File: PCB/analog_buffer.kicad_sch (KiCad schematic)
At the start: 12 parts

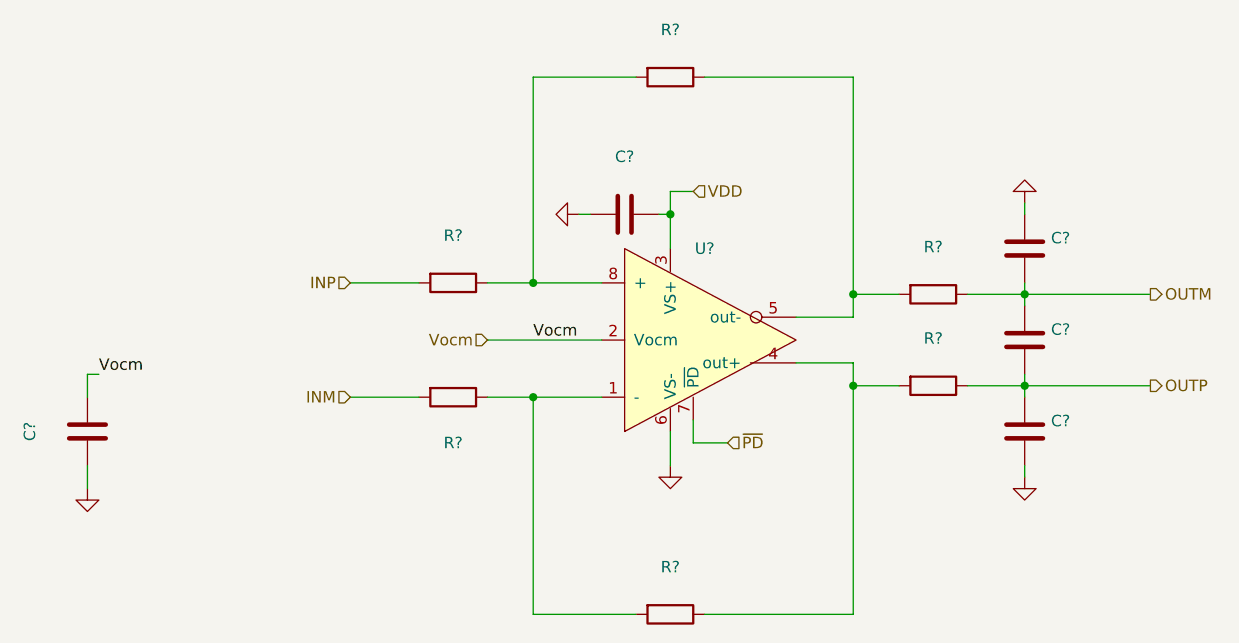
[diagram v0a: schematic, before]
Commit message: New version with FTDI chip instead of STM32 and ICE40HX FPGA instead of slower ones
Signed-off-by: Alexis Jeandet <alexis.jeandet@member.fsf.org>
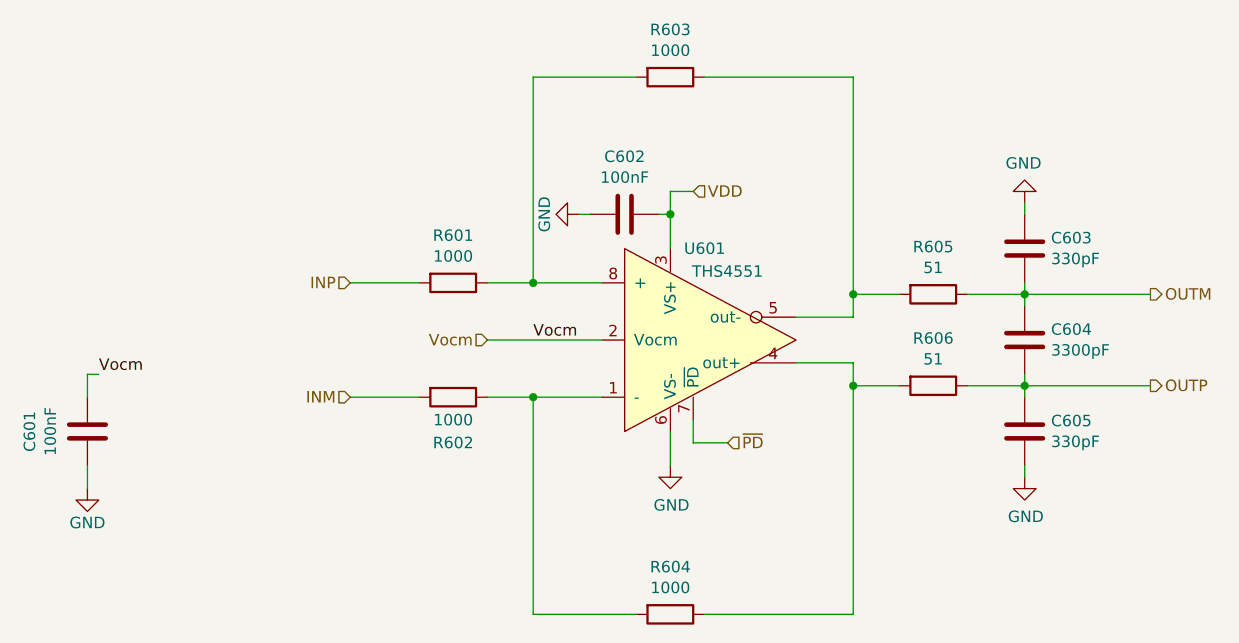
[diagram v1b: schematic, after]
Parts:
- C601: renamed from C?; value (none) -> 100nF; footprint (none) -> Capacitor_SMD:C_0603_1608Metric_Pad1.05x0.95mm_HandSolder
- C602: renamed from C?; value (none) -> 100nF; footprint (none) -> Resistor_SMD:R_0603_1608Metric_Pad1.05x0.95mm_HandSolder
- C603, C605: renamed from C?; value (none) -> 330pF; footprint (none) -> Capacitor_SMD:C_0603_1608Metric_Pad1.05x0.95mm_HandSolder
- C604: renamed from C?; value (none) -> 3300pF; footprint (none) -> Capacitor_SMD:C_0603_1608Metric_Pad1.05x0.95mm_HandSolder
- R601, R602, R603, R604: renamed from R?; value (none) -> 1000; footprint (none) -> Resistor_SMD:R_0603_1608Metric_Pad1.05x0.95mm_HandSolder
- R605, R606: renamed from R?; value (none) -> 51; footprint (none) -> Resistor_SMD:R_0603_1608Metric_Pad1.05x0.95mm_HandSolder
- U601: renamed from U?; value (none) -> THS4551; footprint (none) -> Package_SO:VSSOP-8_3.0x3.0mm_P0.65mm
